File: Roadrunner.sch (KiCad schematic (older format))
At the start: 59 parts, among them J1 USB_OTG, J10 Digital, J11 ~WAKE, J12 Power, J13 SERIAL 4, J14 SERIAL 3, J15 -AREF, J16 +AREF, J17 SPI 2 (D22,D23), J18 Ground, J19 SERIAL 2, J2 JTAG, J20 SPI 0, J21 SERIAL 1, J3 ~RST, J4 PF4, J5 ~HIB, J6 VIn, J7 Power, J8 Analog, J9 Digital, Q1 UM6K33N, Q2 UM6K33N, SW1 RESET, T1 M_Hole, T2 M_Hole, T3 M_Hole, T4 M_Hole, U1 TM4C123GH6PM, U2 LM1117-3.3, Y1 32.768Khz, Y2 16MHz

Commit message: Sweeping changes to board layout.
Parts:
- C1, C10, C12, C13, C14, C15, C16, C2, C3, C4, C5, C6, C7, C8, C9: symbol C_Small -> Device:C_Small
- C11, C17: symbol CP -> Device:CP
- D2, D3, D4, D5: symbol LED_ALT -> Device:LED_ALT
- J1: symbol USB_OTG -> conn:USB_OTG
- J10, J7: symbol CONN_01X08 -> Roadrunner-rescue:CONN_01X08
- J11, J3, J5: symbol HEADER_1 -> Roadrunner-rescue:HEADER_1
- J12, J18, J2, J20: symbol CONN_01X04 -> Roadrunner-rescue:CONN_01X04
- J13, J14, J15, J16, J17, J19, J21, J6: symbol CONN_01X02 -> Roadrunner-rescue:CONN_01X02
- J4: symbol CONN_01X01 -> Roadrunner-rescue:CONN_01X01
- J8: symbol CONN_01X06 -> Roadrunner-rescue:CONN_01X06
- J9: symbol CONN_01X10 -> Roadrunner-rescue:CONN_01X10
- Q1, Q2: symbol UM6K33N -> Roadrunner-rescue:UM6K33N
- R1, R2, R5, R6: symbol R -> Device:R
- RN1, RN2: symbol R_Pack04 -> Device:R_Pack04
- SW1: symbol SW_PUSH -> Roadrunner-rescue:SW_PUSH
- T1, T2, T3, T4: symbol M_Hole -> Roadrunner-rescue:M_Hole
- U1: symbol TM4C123GH6PM -> tm4c123gh6pm:TM4C123GH6PM
- U2: symbol LM1117-3.3 -> regul:LM1117-3.3
- Y1, Y2: symbol Crystal -> Device:Crystal
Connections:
- net labels added: D10_SS_1, D11_TX_1, D12_RX_1, D13_CLK_1, SSI_CLK_0, SSI_RX_0, SSI_SS_0, SSI_TX_0
- net labels removed: PA2, PA3, PA4, PA5
- wire segments 209 -> 258
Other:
- note added: "3.3V Power Supply for Microcontroller"
- note added: "Additional Power and Ground Connections"
- note added: "Arduino Headers"
- note added: "LED Indicators"
- note added: "Mounting Holes"
- note added: "Power Inputs"
- note added: "Switches"
- note added: "USB Input Connector"
- note added: "VDD Supply Filter Caps"
- moved on the sheet: C10, C11, C15, C16, C17, C5, C6, C7, C8, C9, J1, J11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

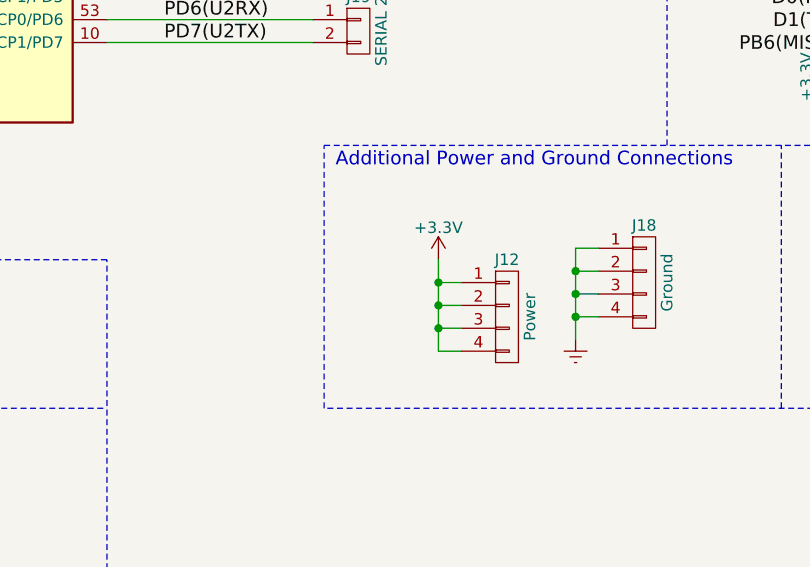
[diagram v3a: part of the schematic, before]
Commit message: Swapped some 3.3v outputs on rear header for 5V.
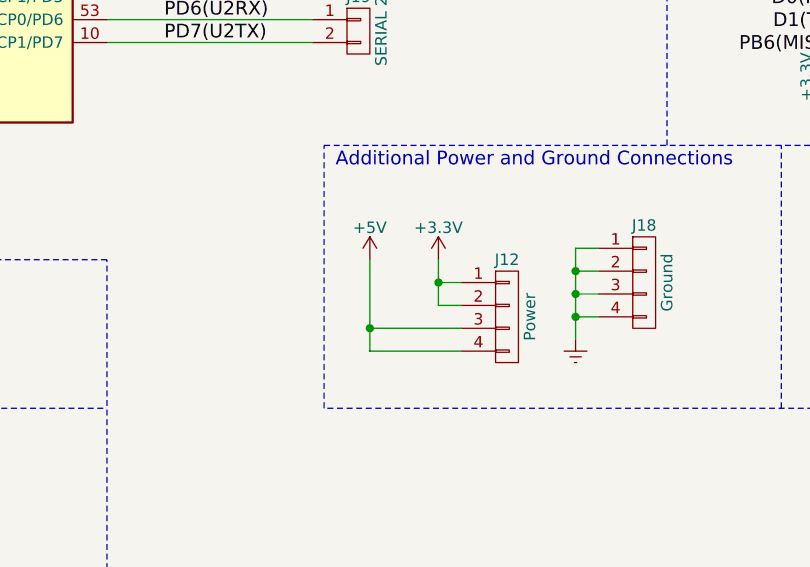
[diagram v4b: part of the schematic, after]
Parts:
- C15, C5, C7, C9: Description 6.3 V to 25 V, X5R/X7R ceramic chip -> CAP CER 0.1UF 25V X7R 0603
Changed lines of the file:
@@
 Sheet 1 1
 Title "Roadrunner"
-Date "2017-08-19"
+Date "2019-01-08"
 Rev "v1.2"
 Comp "Jacob Miller"
@@
 F 2 "Capacitors_SMD:C_0603" H 1100 2750 50  0001 C CNN
 F 3 "http://www.yageo.com/documents/recent/UPY-GPHC_X7R_6.3V-to-50V_17.pdf" H 1100 2750 50  0001 C CNN
-F 4 "6.3 V to 25 V, X5R/X7R ceramic chip" H 1100 2750 60  0001 C CNN "Description"
+F 4 "CAP CER 0.1UF 25V X7R 0603" H 1100 2750 60  0001 C CNN "Description"
 F 5 "CC0603JRX7R8BB104" H 1100 2750 60  0001 C CNN "Part #"
 	1    1100 2750
@@
 F 1 "22.0uF" H 2010 2670 50  0000 L CNN
 F 2 "Capacitors_SMD:C_0805" H 2000 2750 50  0001 C CNN
-F 3 "" H 2000 2750 50  0001 C CNN
+F 3 "http://www.samsungsem.com/kr/support/library/product-catalog/__icsFiles/afieldfile/2016/09/27/MLCC.pdf" H 2000 2750 50  0001 C CNN
 F 4 "6.3 V to 25 V, X5R/X7R ceramic chip" H 2000 2750 60  0001 C CNN "Description"
 F 5 "CL21A226MOCLRNC" H 2000 2750 60  0001 C CNN "Part #"
@@
 F 1 "22.0uF" H 1410 3270 50  0000 L CNN
 F 2 "Capacitors_SMD:C_0805" H 1400 3350 50  0001 C CNN
-F 3 "" H 1400 3350 50  0001 C CNN
+F 3 "http://www.samsungsem.com/kr/support/library/product-catalog/__icsFiles/afieldfile/2016/09/27/MLCC.pdf" H 1400 3350 50  0001 C CNN
 F 4 "6.3 V to 25 V, X5R/X7R ceramic chip" H 1400 3350 60  0001 C CNN "Description"
 F 5 "CL21A226MOCLRNC" H 1400 3350 60  0001 C CNN "Part #"
@@
 F 1 "0.1uF" H 1710 2670 50  0000 L CNN
 F 2 "Capacitors_SMD:C_0603" H 1700 2750 50  0001 C CNN
-F 3 "" H 1700 2750 50  0001 C CNN
-F 4 "6.3 V to 25 V, X5R/X7R ceramic chip" H 1700 2750 60  0001 C CNN "Description"
+F 3 "http://www.yageo.com/documents/recent/UPY-GPHC_X7R_6.3V-to-50V_17.pdf" H 1700 2750 50  0001 C CNN
+F 4 "CAP CER 0.1UF 25V X7R 0603" H 1700 2750 60  0001 C CNN "Description"
 F 5 "CC0603JRX7R8BB104" H 1700 2750 60  0001 C CNN "Part #"
 	1    1700 2750
@@
 F 1 "0.1uF" H 1110 3270 50  0000 L CNN
 F 2 "Capacitors_SMD:C_0603" H 1100 3350 50  0001 C CNN
-F 3 "" H 1100 3350 50  0001 C CNN
-F 4 "6.3 V to 25 V, X5R/X7R ceramic chip" H 1100 3350 60  0001 C CNN "Description"
+F 3 "http://www.yageo.com/documents/recent/UPY-GPHC_X7R_6.3V-to-50V_17.pdf" H 1100 3350 50  0001 C CNN
+F 4 "CAP CER 0.1UF 25V X7R 0603" H 1100 3350 60  0001 C CNN "Description"
 F 5 "CC0603JRX7R8BB104" H 1100 3350 60  0001 C CNN "Part #"
 	1    1100 3350
@@
 F 1 "22.0uF" H 2010 3270 50  0000 L CNN
 F 2 "Capacitors_SMD:C_0805" H 2000 3350 50  0001 C CNN
-F 3 "" H 2000 3350 50  0001 C CNN
+F 3 "http://www.samsungsem.com/kr/support/library/product-catalog/__icsFiles/afieldfile/2016/09/27/MLCC.pdf" H 2000 3350 50  0001 C CNN
 F 4 "6.3 V to 25 V, X5R/X7R ceramic chip" H 2000 3350 60  0001 C CNN "Description"
 F 5 "CL21A226MOCLRNC" H 2000 3350 60  0001 C CNN "Part #"
@@
 F 1 "0.1uF" H 1710 3270 50  0000 L CNN
 F 2 "Capacitors_SMD:C_0603" H 1700 3350 50  0001 C CNN
-F 3 "" H 1700 3350 50  0001 C CNN
-F 4 "6.3 V to 25 V, X5R/X7R ceramic chip" H 1700 3350 60  0001 C CNN "Description"
+F 3 "http://www.yageo.com/documents/recent/UPY-GPHC_X7R_6.3V-to-50V_17.pdf" H 1700 3350 50  0001 C CNN
+F 4 "CAP CER 0.1UF 25V X7R 0603" H 1700 3350 60  0001 C CNN "Description"
 F 5 "CC0603JRX7R8BB104" H 1700 3350 60  0001 C CNN "Part #"
 	1    1700 3350
@@
 	8300 5850 8300 5950
 Wire Wire Line
-	8300 6250 8400 6250
-Wire Wire Line
-	8400 6150 8300 6150
-Connection ~ 8300 6150
-Wire Wire Line
 	8400 6050 8300 6050
-Connection ~ 8300 6050
 Wire Wire Line
 	8400 5950 8300 5950
@@
 	8900 6100 8900 6000
 Wire Wire Line
-	8300 6150 8300 6250
-Wire Wire Line
-	8300 6050 8300 6150
-Wire Wire Line
 	8300 5950 8300 6050
 Wire Wire Line
@@
 Wire Notes Line
 	7800 5350 11200 5350
+$Comp
+L power:+5V #PWR0101
+U 1 1 5C369140
+P 8000 5850
+F 0 "#PWR0101" H 8000 5700 50  0001 C CNN
+F 1 "+5V" H 8000 5990 50  0000 C CNN
+F 2 "" H 8000 5850 50  0001 C CNN
+F 3 "" H 8000 5850 50  0001 C CNN
+	1    8000 5850
+	1    0    0    -1
+$EndComp
+Wire Wire Line
+	8400 6150 8000 6150
+Wire Wire Line
+	8000 6150 8000 5850
+Wire Wire Line
+	8400 6250 8000 6250
+Wire Wire Line
+	8000 6250 8000 6150
+Connection ~ 8000 6150
 $EndSCHEMATC
